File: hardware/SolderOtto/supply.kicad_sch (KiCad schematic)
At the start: 53 parts, among them J201 Conn_02x04_Counter_Clockwise, Q201 T2N7002AK, Q202 BC858B, Q203 BC847A, Q204 BC847A, U201 LM5012, U202 LM337_TO252, U203 LM317_TO-252, U206 MCP9701T-E/TT

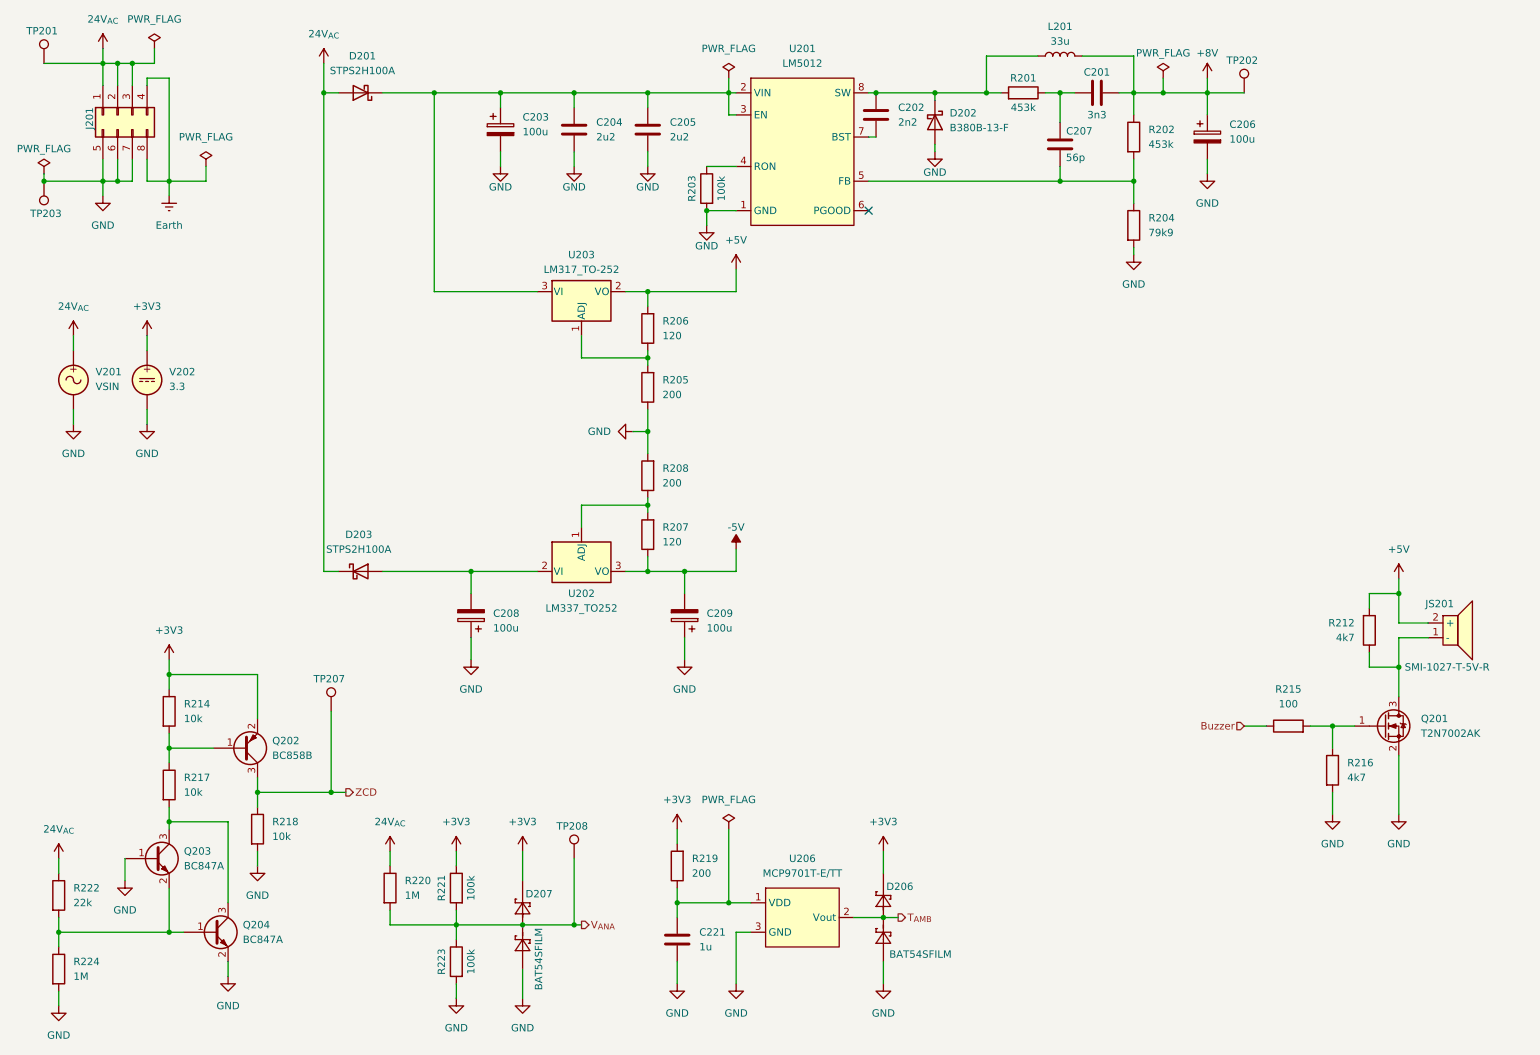
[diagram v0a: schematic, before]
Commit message: remove 12V rail
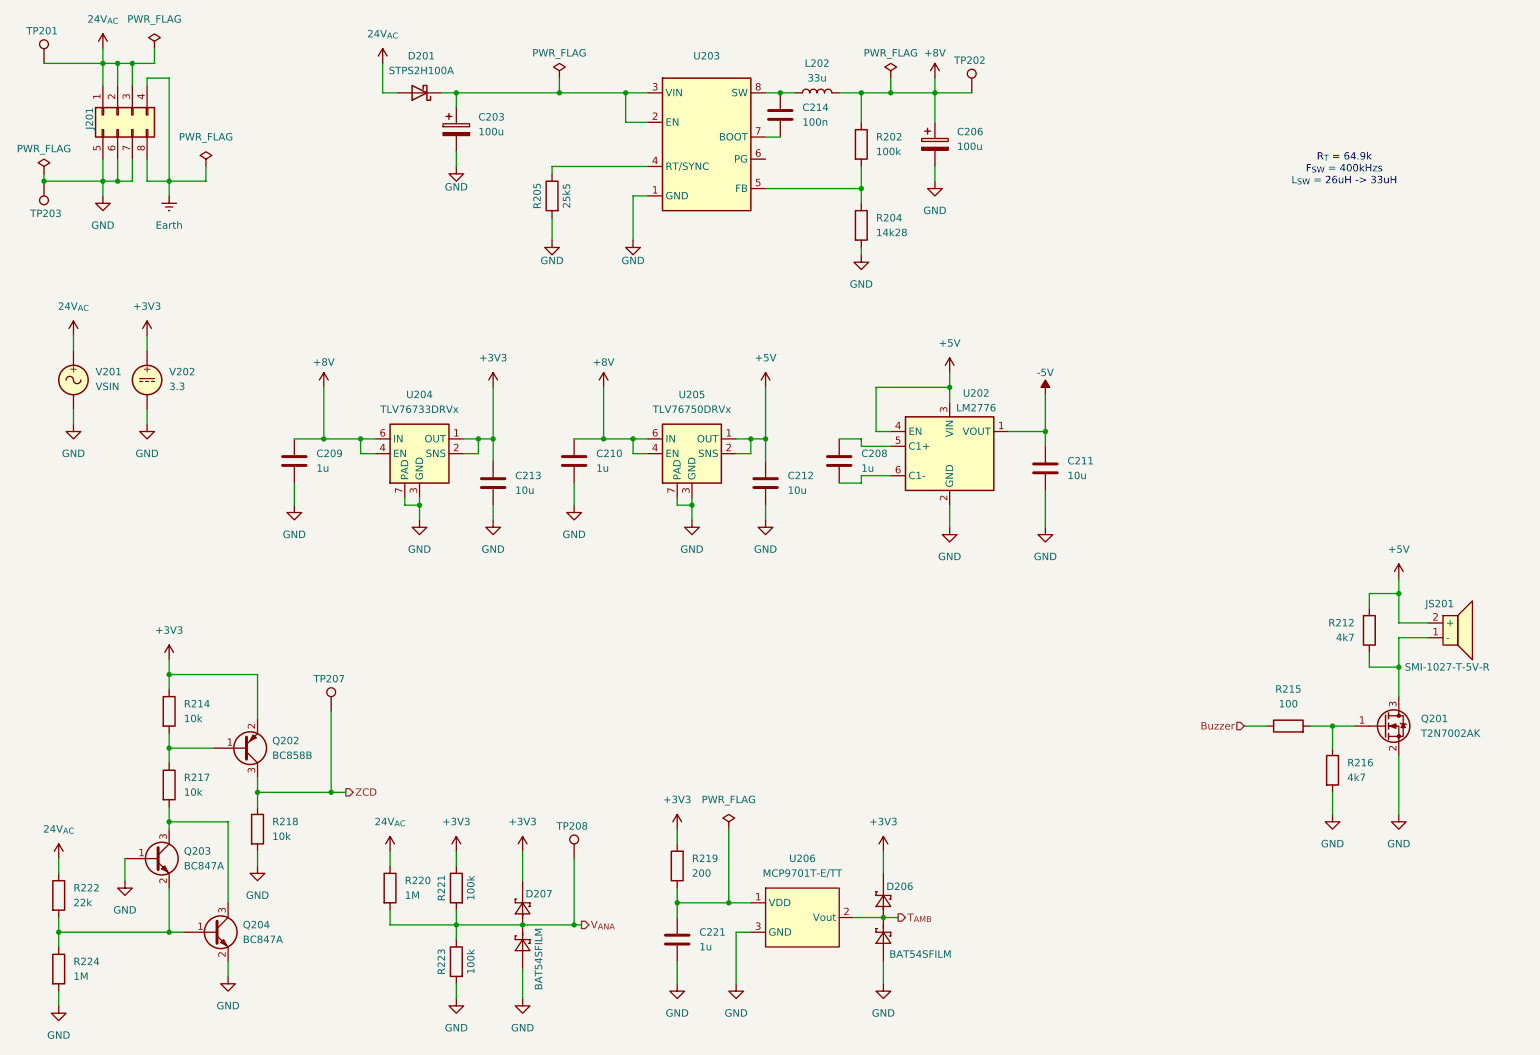
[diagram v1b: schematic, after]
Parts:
- removed C201: 3n3, Capacitor_SMD:C_0603_1608Metric, symbol Device:C
- removed C202: 2n2, Capacitor_SMD:C_0603_1608Metric, symbol Device:C
- removed C204, C205: 2u2, Capacitor_SMD:C_1206_3216Metric, symbol Device:C
- removed C207: 56p, Capacitor_SMD:C_0603_1608Metric, symbol Device:C
- removed C208, C209: 100u, mylib_common:CP_Elec_10x10.5_A768, symbol Device:C_Polarized
- removed D202: B380B-13-F, Diode_SMD:D_SMB, symbol Device:D_Schottky
- removed D203: STPS2H100A, Diode_SMD:D_SMA, symbol Device:D_Schottky
- removed L201: 33u, Inductor_SMD:L_Taiyo-Yuden_NR-80xx, symbol Device:L
- removed R201: 453k, Resistor_SMD:R_0603_1608Metric, symbol Device:R
- removed R203: 100k, Resistor_SMD:R_0603_1608Metric, symbol Device:R
- removed R206, R207: 120, Resistor_SMD:R_0603_1608Metric, symbol Device:R
- removed R208: 200, Resistor_SMD:R_0603_1608Metric, symbol Device:R
- removed U201: LM5012, Package_SO:TI_SO-PowerPAD-8, symbol mylib_pmic:LM5012DDAR
- removed U202: LM337_TO252, Package_TO_SOT_SMD:TO-252-2, symbol Regulator_Linear:LM337_TO252
- removed U203: LM317_TO-252, Package_TO_SOT_SMD:TO-252-2, symbol Regulator_Linear:LM317_TO-252
- added C208, C209, C210: 1u, Capacitor_SMD:C_0603_1608Metric, symbol Device:C
- added C211, C212, C213: 10u, Capacitor_SMD:C_0603_1608Metric, symbol Device:C
- added C214: 100n, Capacitor_SMD:C_0603_1608Metric, symbol Device:C
- added L202: 33u, Inductor_SMD:L_Taiyo-Yuden_NR-80xx, symbol Device:L
- added U202: LM2776, Package_TO_SOT_SMD:SOT-23-6, symbol Regulator_SwitchedCapacitor:LM2776
- added U203: ~, Package_SO:TI_SO-PowerPAD-8, symbol mylib_pmic:LMR38010
- added U204: TLV76733DRVx, Package_SON:WSON-6-1EP_2x2mm_P0.65mm_EP1x1.6mm_ThermalVias, symbol Regulator_Linear:TLV76733DRVx
- added U205: TLV76750DRVx, Package_SON:WSON-6-1EP_2x2mm_P0.65mm_EP1x1.6mm_ThermalVias, symbol Regulator_Linear:TLV76750DRVx
- R202: value 453k -> 100k
- R204: value 79k9 -> 14k28
- R205: value 200 -> 25k5
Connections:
- net +3V3: now also C213.1, U204.1 (OUT), U204.2 (SNS)
- net +5V: now also C212.1, U202.3 (VIN), U202.4 (EN), U205.1 (OUT), U205.2 (SNS)
- net +8V: now also C209.1, C210.1, L202.2, U204.4 (EN), U204.6 (IN), U205.4 (EN), U205.6 (IN)
- net -5V: now also C211.1, U202.1 (VOUT)
- net GND: now also R205.2, C209.2, C210.2, C211.2, C212.2, C213.2, U202.2 (GND), U203.1 (GND), U203.9 (GND), U204.3 (GND), U204.5 (GND), U204.7 (PAD), U205.3 (GND), U205.5 (GND), U205.7 (PAD); no longer R205.1
- net at C203.1, D201.1 (K): now also U203.2 (EN), U203.3 (VIN)
- net at R202.2, R204.1: now also U203.5 (FB)
- new net: C208.1, U202.5 (C1+)
- new net: C208.2, U202.6 (C1-)
- new net: C214.1, L202.1, U203.8 (SW)
- new net: C214.2, U203.7 (BOOT)
- new net: R205.1, U203.4 (RT/SYNC)
- no-connect marks 1 -> 0
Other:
- note added: "R_{T} = 64.9k F_{SW} = 400kHzs L_{SW} = 26uH -> 33uH"
- moved on the sheet: C203, C206, D201, R202, R204, TP202

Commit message: save work
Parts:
- added TP204, TP205, TP206: 12V, TestPoint:TestPoint_Keystone_5015_Micro-Minature, symbol Connector:TestPoint
- R211: renamed from R220; value 1M -> 1M15; Digikey P1.00MHCT-ND -> 13-RC0603FR-071M15LCT-ND
- U201: renamed from U203; value ~ -> LMR38010
- renumbered C214 to C201, C203 to C202, C206 to C203, C209 to C204, C210 to C205, C208 to C206, C211 to C207, C213 to C208, C212 to C209, C221 to C210, D206 to D202, D207 to D203, L202 to L201, R202 to R201, R205 to R202, R204 to R203, R212 to R204, R214 to R205, R215 to R206, R216 to R207, R217 to R208, R218 to R209, R219 to R210, R221 to R212, R222 to R213, R223 to R214, R224 to R215, U204 to U203, U205 to U204, U206 to U205
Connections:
- net +3V3: now also TP205.1
- net +5V: now also TP206.1
- net -5V: now also TP204.1

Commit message: rdy to route
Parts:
- R201: Digikey P453KHCT-ND -> 311-100KHRCT-ND
- R202: Digikey (none) -> 311-25.5KCRCT-ND
- R203: value 14k28 -> 14k3; Digikey (none) -> RMCF0603FT14K3CT-ND
- U201: Digikey (none) -> 296-LMR38010FDDARCT-ND
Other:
- moved on the sheet: C204, C205

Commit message: save some stuff
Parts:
- renumbered C206 to C204, C207 to C205, C204 to C206, C205 to C207
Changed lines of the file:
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@@
 		(on_board yes)
 		(dnp no)
-		(property "Reference" "#PWR0214"
+		(property "Reference" "#PWR0215"
 			(at 68.58 87.63 0)
 			(effects
@@
 			(project "SolderOtto"
 				(path "/04e99464-bf33-4a4f-8397-d26b5ec904f3/1f74b07f-4a28-48ba-be90-ad5de8d466f3"
-					(reference "#PWR0214")
+					(reference "#PWR0215")
 					(unit 1)
 				)
@@
 		(on_board yes)
 		(dnp no)
-		(property "Reference" "C204"
+		(property "Reference" "C206"
 			(at 72.39 95.2499 0)
 			(effects
@@
 			(project "SolderOtto"
 				(path "/04e99464-bf33-4a4f-8397-d26b5ec904f3/1f74b07f-4a28-48ba-be90-ad5de8d466f3"
-					(reference "C204")
+					(reference "C206")
 					(unit 1)
 				)
@@
 		(dnp no)
 		(fields_autoplaced yes)
-		(property "Reference" "#PWR0222"
+		(property "Reference" "#PWR0224"
 			(at 115.57 110.49 0)
 			(effects
@@
 			(project "SolderOtto"
 				(path "/04e99464-bf33-4a4f-8397-d26b5ec904f3/1f74b07f-4a28-48ba-be90-ad5de8d466f3"
-					(reference "#PWR0222")
+					(reference "#PWR0224")
 					(unit 1)
 				)
@@
 		(on_board yes)
 		(dnp no)
-		(property "Reference" "#PWR0216"
+		(property "Reference" "#PWR0217"
 			(at 115.57 87.63 0)
 			(effects
@@
 			(project "SolderOtto"
 				(path "/04e99464-bf33-4a4f-8397-d26b5ec904f3/1f74b07f-4a28-48ba-be90-ad5de8d466f3"
-					(reference "#PWR0216")
+					(reference "#PWR0217")
 					(unit 1)
 				)
@@
 		(on_board yes)
 		(dnp no)
-		(property "Reference" "C206"
+		(property "Reference" "C204"
 			(at 160.02 92.7099 0)
 			(effects
@@
 			(project "SolderOtto"
 				(path "/04e99464-bf33-4a4f-8397-d26b5ec904f3/1f74b07f-4a28-48ba-be90-ad5de8d466f3"
-					(reference "C206")
+					(reference "C204")
 					(unit 1)
 				)
@@
 		(dnp no)
 		(fields_autoplaced yes)
-		(property "Reference" "#PWR0215"
+		(property "Reference" "#PWR0216"
 			(at 96.52 87.63 0)
 			(effects
@@
 			(project "SolderOtto"
 				(path "/04e99464-bf33-4a4f-8397-d26b5ec904f3/1f74b07f-4a28-48ba-be90-ad5de8d466f3"
-					(reference "#PWR0215")
+					(reference "#PWR0216")
 					(unit 1)
 				)
@@
 		(dnp no)
 		(fields_autoplaced yes)
-		(property "Reference" "C207"
+		(property "Reference" "C205"
 			(at 195.58 93.9799 0)
 			(effects
@@
 			(project "SolderOtto"
 				(path "/04e99464-bf33-4a4f-8397-d26b5ec904f3/1f74b07f-4a28-48ba-be90-ad5de8d466f3"
-					(reference "C207")
+					(reference "C205")
 					(unit 1)
 				)
@@
 		(dnp no)
 		(fields_autoplaced yes)
-		(property "Reference" "C205"
+		(property "Reference" "C207"
 			(at 119.38 95.2499 0)
 			(effects
@@
 			(project "SolderOtto"
 				(path "/04e99464-bf33-4a4f-8397-d26b5ec904f3/1f74b07f-4a28-48ba-be90-ad5de8d466f3"
-					(reference "C205")
+					(reference "C207")
 					(unit 1)
 				)
@@
 		(on_board yes)
 		(dnp no)
-		(property "Reference" "#PWR0218"
+		(property "Reference" "#PWR0214"
 			(at 191.77 86.36 0)
 			(effects
@@
 			(project "SolderOtto"
 				(path "/04e99464-bf33-4a4f-8397-d26b5ec904f3/1f74b07f-4a28-48ba-be90-ad5de8d466f3"
-					(reference "#PWR0218")
+					(reference "#PWR0214")
 					(unit 1)
 				)
@@
 		(dnp no)
 		(fields_autoplaced yes)
-		(property "Reference" "#PWR0217"
+		(property "Reference" "#PWR0218"
 			(at 143.51 87.63 0)
 			(effects
@@
 			(project "SolderOtto"
 				(path "/04e99464-bf33-4a4f-8397-d26b5ec904f3/1f74b07f-4a28-48ba-be90-ad5de8d466f3"
-					(reference "#PWR0217")
+					(reference "#PWR0218")
 					(unit 1)
 				)
@@
 		(dnp no)
 		(fields_autoplaced yes)
-		(property "Reference" "#PWR0224"
+		(property "Reference" "#PWR0223"
 			(at 96.52 110.49 0)
 			(effects
@@
 			(project "SolderOtto"
 				(path "/04e99464-bf33-4a4f-8397-d26b5ec904f3/1f74b07f-4a28-48ba-be90-ad5de8d466f3"
-					(reference "#PWR0224")
+					(reference "#PWR0223")
 					(unit 1)
 				)
@@
 		(dnp no)
 		(fields_autoplaced yes)
-		(property "Reference" "#PWR0223"
+		(property "Reference" "#PWR0222"
 			(at 83.82 110.49 0)
 			(effects
@@
 			(project "SolderOtto"
 				(path "/04e99464-bf33-4a4f-8397-d26b5ec904f3/1f74b07f-4a28-48ba-be90-ad5de8d466f3"
-					(reference "#PWR0223")
+					(reference "#PWR0222")
 					(unit 1)
 				)
